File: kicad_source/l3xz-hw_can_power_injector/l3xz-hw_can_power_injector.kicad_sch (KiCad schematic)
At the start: 18 parts, among them CN1 Conn_01x02, CN2 Conn_01x04, CN3 Conn_01x04, CN4 Conn_01x02, U1 RAA211650

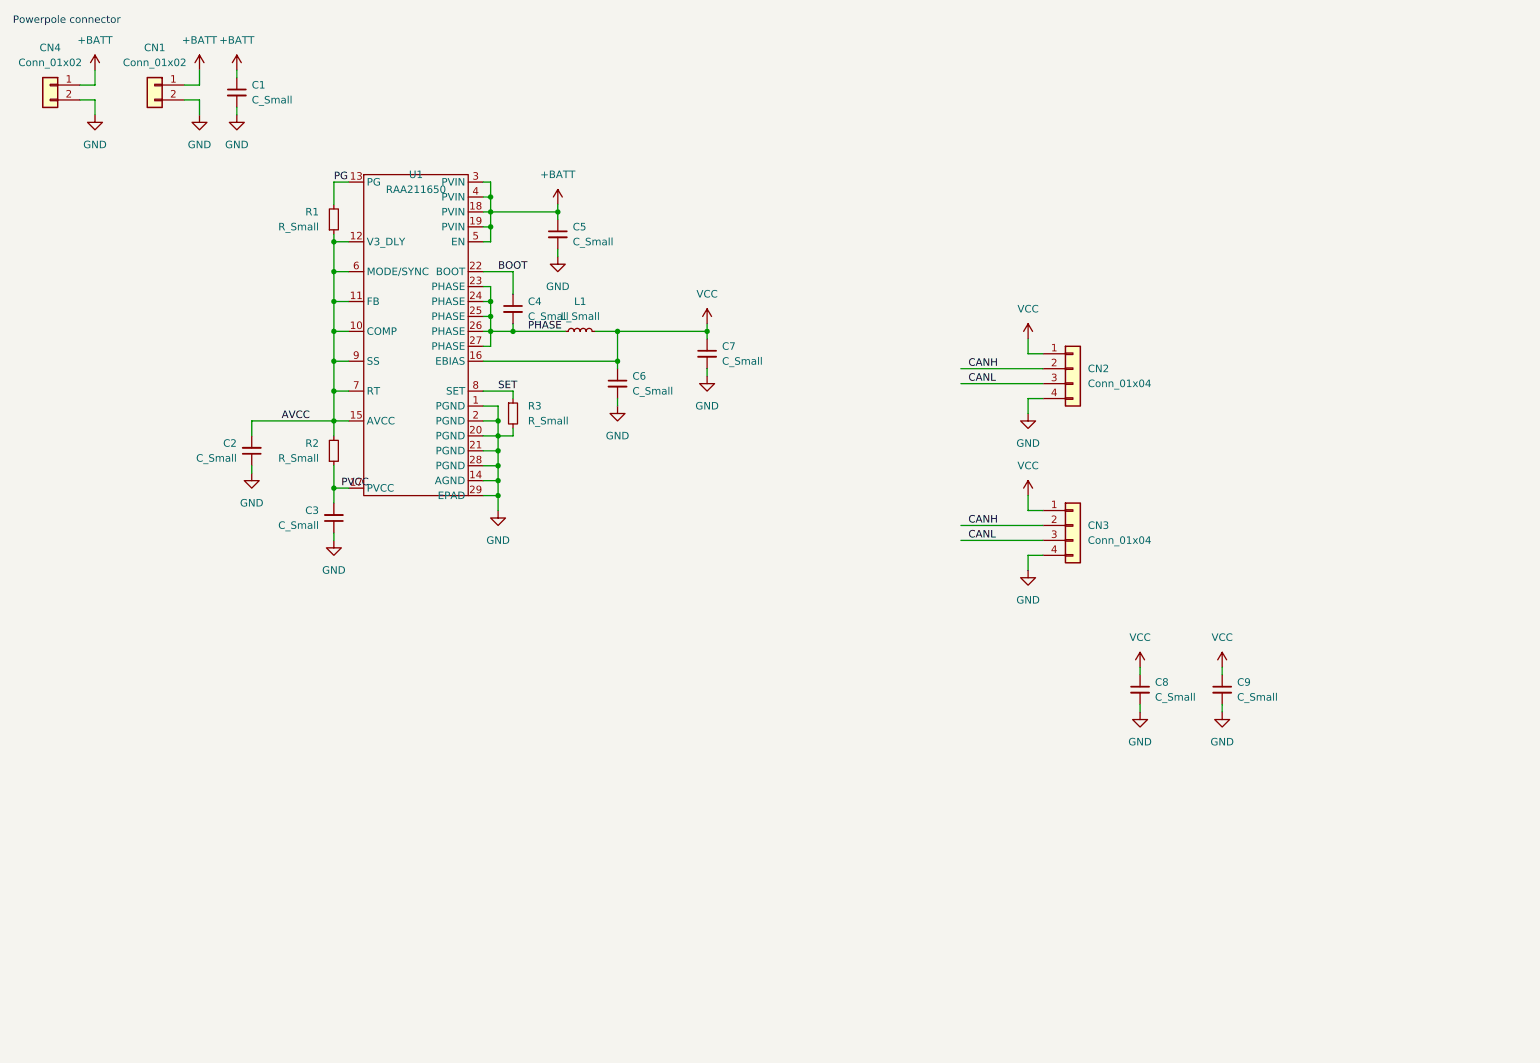
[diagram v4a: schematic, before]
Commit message: addedhoricontal powerpole
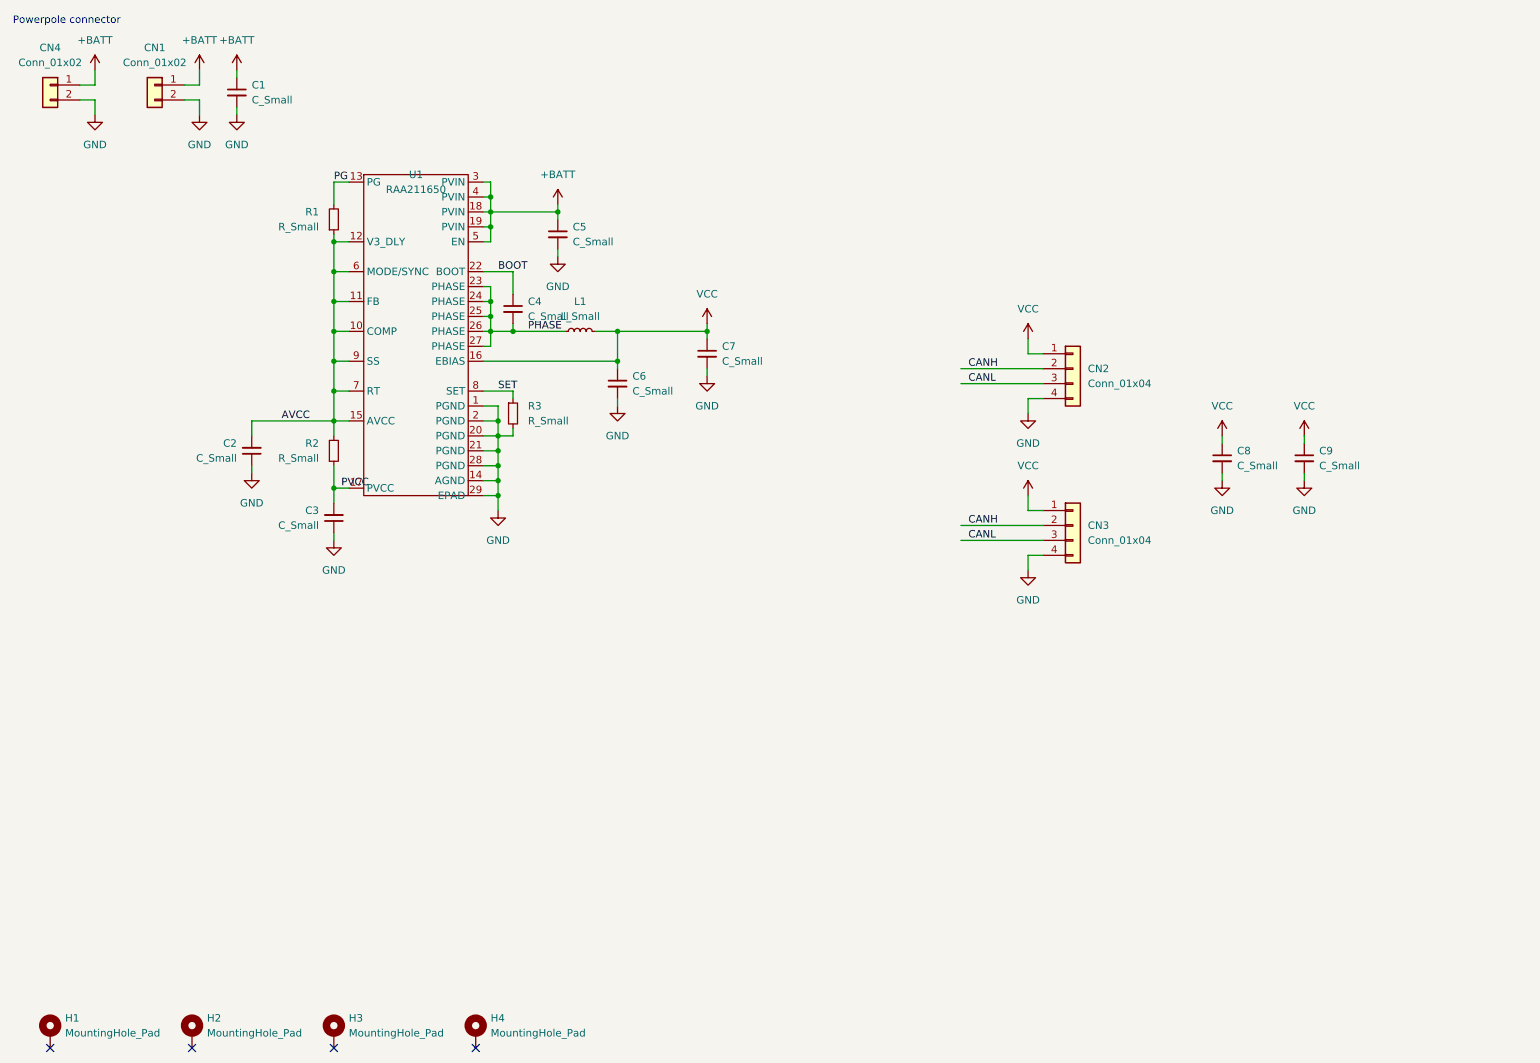
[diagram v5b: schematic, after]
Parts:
- added H1, H2, H3, H4: MountingHole_Pad, MountingHole:MountingHole_3.2mm_M3_DIN965_Pad, symbol Mechanical:MountingHole_Pad
- CN4: footprint generationmake:POWERPOLE_2 -> generationmake:POWERPOLE_hor_2
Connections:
- no-connect marks 0 -> 4
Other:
- moved on the sheet: C8, C9

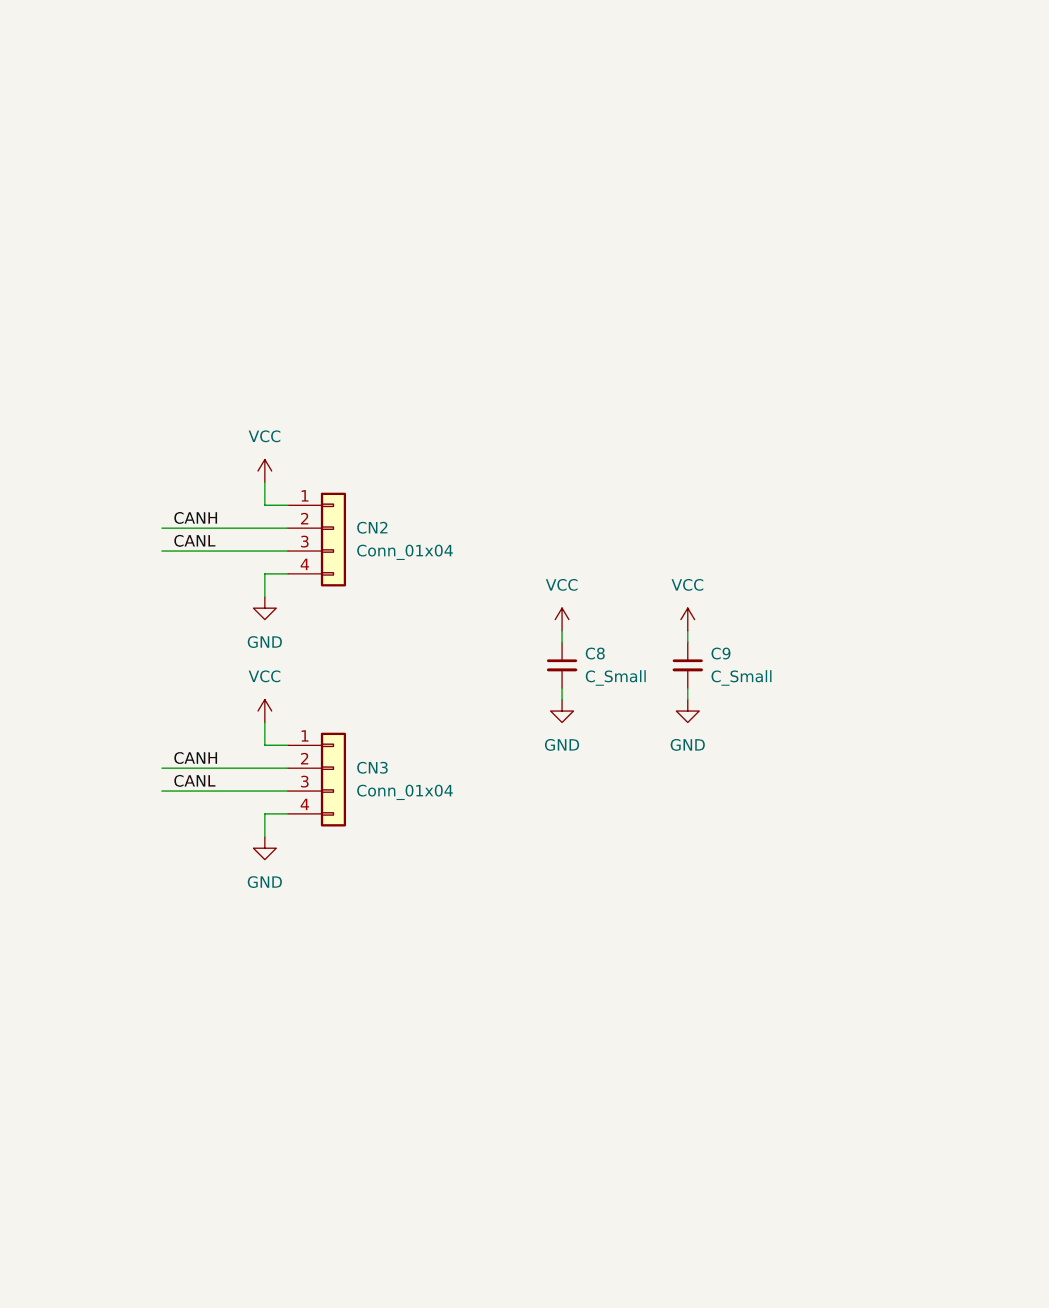
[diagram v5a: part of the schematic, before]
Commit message: added second uavcan channel and diodes
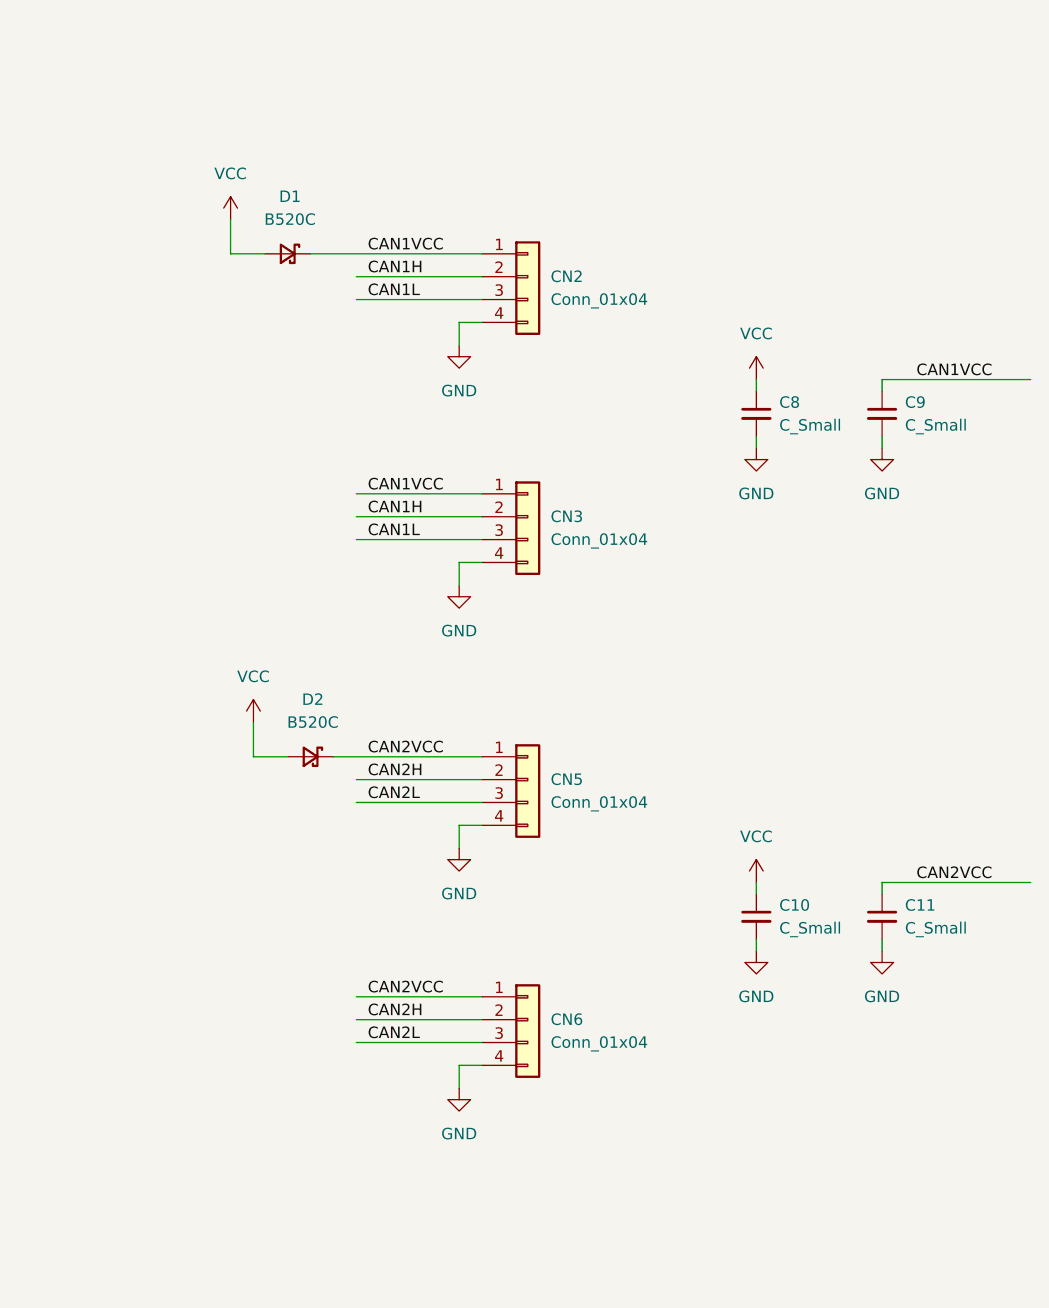
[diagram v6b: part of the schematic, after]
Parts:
- added C10: C_Small, Capacitor_SMD:C_1210_3225Metric, symbol Device:C_Small
- added C11: C_Small, Capacitor_SMD:C_0603_1608Metric, symbol Device:C_Small
- added CN5, CN6: Conn_01x04, Connector_JST:JST_GH_BM04B-GHS-TBT_1x04-1MP_P1.25mm_Vertical, symbol Connector_Generic:Conn_01x04
- added D1, D2: B520C, Diode_SMD:D_SMC, symbol Device:D_Schottky_Small
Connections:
- net GND: now also C10.2, C11.2, CN5.4 (Pin_4), CN6.4 (Pin_4)
- net VCC: now also C10.1, D1.2 (A), D2.2 (A); no longer C9.1, CN2.1 (Pin_1), CN3.1 (Pin_1)
- net CANH renamed CAN1H
- net CANL renamed CAN1L
- new net CAN1VCC: C9.1, CN2.1 (Pin_1), CN3.1 (Pin_1), D1.1 (K)
- new net CAN2H: CN5.2 (Pin_2), CN6.2 (Pin_2)
- new net CAN2L: CN5.3 (Pin_3), CN6.3 (Pin_3)
- new net CAN2VCC: C11.1, CN5.1 (Pin_1), CN6.1 (Pin_1), D2.1 (K)
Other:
- moved on the sheet: C8, C9, CN2, CN3

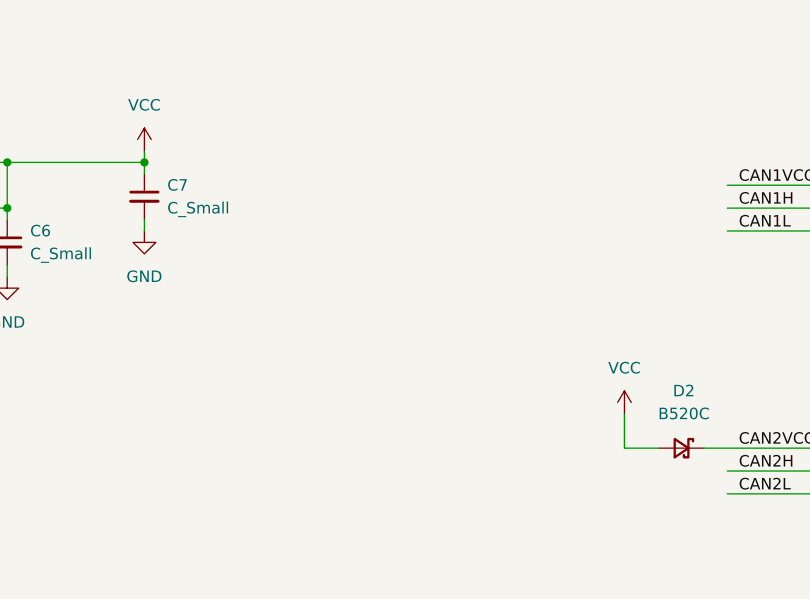
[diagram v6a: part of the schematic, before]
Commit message: added LED
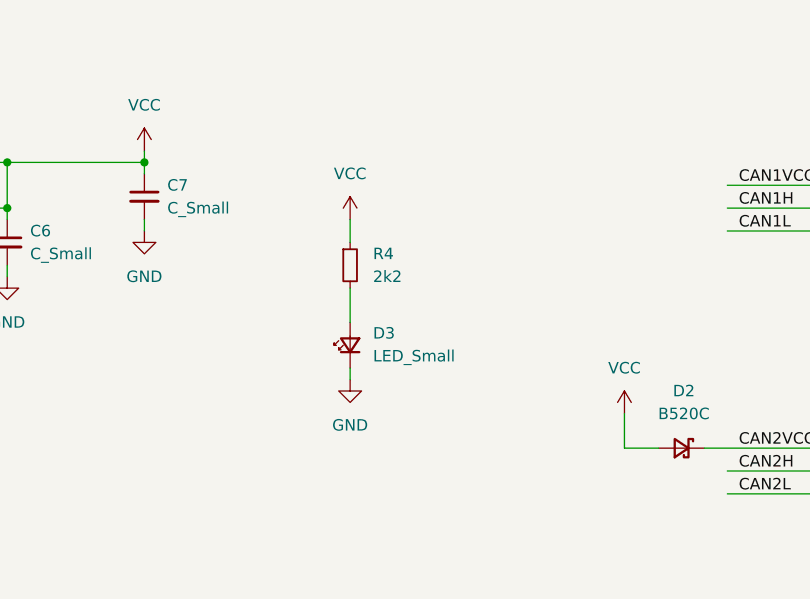
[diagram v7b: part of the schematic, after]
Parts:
- added D3: LED_Small, LED_SMD:LED_0603_1608Metric, symbol Device:LED_Small
- added R4: 2k2, Resistor_SMD:R_0603_1608Metric, symbol Device:R_Small
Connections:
- net GND: now also D3.1 (K)
- net VCC: now also R4.1
- new net: D3.2 (A), R4.2
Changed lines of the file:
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@@
+    (stroke (width 0) (type default) (color 0 0 0 0))
+  )
+  (wire (pts (xy 156.21 83.82) (xy 156.21 87.63))
     (stroke (width 0) (type default) (color 0 0 0 0))
   )
@@
     (stroke (width 0) (type default) (color 0 0 0 0))
   )
+  (wire (pts (xy 156.21 92.71) (xy 156.21 93.98))
+    (stroke (width 0) (type default) (color 0 0 0 0))
+  )
   (wire (pts (xy 96.52 52.07) (xy 96.52 49.53))
     (stroke (width 0) (type default) (color 0 0 0 0))
@@
   )
   (wire (pts (xy 198.12 48.26) (xy 212.09 48.26))
+    (stroke (width 0) (type default) (color 0 0 0 0))
+  )
+  (wire (pts (xy 156.21 76.2) (xy 156.21 78.74))
     (stroke (width 0) (type default) (color 0 0 0 0))
   )
@@
     )
     (property "Datasheet" "~" (id 3) (at 69.85 101.6 0)
+      (effects (font (size 1.27 1.27)) hide)
+    )
+    (pin "1")
+    (pin "2")
+  )
+  (symbol (lib_id "Device:LED_Small") (at 156.21 90.17 90) (unit 1)
+    (in_bom yes) (on_board yes) (fields_autoplaced)
+    (property "Reference" "D3" (id 0) (at 158.75 88.8364 90)
+      (effects (font (size 1.27 1.27)) (justify right))
+    )
+    (property "Value" "LED_Small" (id 1) (at 158.75 91.3764 90)
+      (effects (font (size 1.27 1.27)) (justify right))
+    )
+    (property "Footprint" "LED_SMD:LED_0603_1608Metric" (id 2) (at 156.21 90.17 90)
+      (effects (font (size 1.27 1.27)) hide)
+    )
+    (property "Datasheet" "~" (id 3) (at 156.21 90.17 90)
       (effects (font (size 1.27 1.27)) hide)
     )
@@
     (pin "2")
   )
+  (symbol (lib_id "power:VCC") (at 156.21 76.2 0) (unit 1)
+    (in_bom yes) (on_board yes) (fields_autoplaced)
+    (property "Reference" "#PWR019" (id 0) (at 156.21 80.01 0)
+      (effects (font (size 1.27 1.27)) hide)
+    )
+    (property "Value" "VCC" (id 1) (at 156.21 71.12 0))
+    (property "Footprint" "" (id 2) (at 156.21 76.2 0)
+      (effects (font (size 1.27 1.27)) hide)
+    )
+    (property "Datasheet" "" (id 3) (at 156.21 76.2 0)
+      (effects (font (size 1.27 1.27)) hide)
+    )
+    (pin "1")
+  )
+  (symbol (lib_id "power:GND") (at 156.21 93.98 0) (unit 1)
+    (in_bom yes) (on_board yes) (fields_autoplaced)
+    (property "Reference" "#PWR023" (id 0) (at 156.21 100.33 0)
+      (effects (font (size 1.27 1.27)) hide)
+    )
+    (property "Value" "GND" (id 1) (at 156.21 99.06 0))
+    (property "Footprint" "" (id 2) (at 156.21 93.98 0)
+      (effects (font (size 1.27 1.27)) hide)
+    )
+    (property "Datasheet" "" (id 3) (at 156.21 93.98 0)
+      (effects (font (size 1.27 1.27)) hide)
+    )
+    (pin "1")
+  )
   (symbol (lib_id "Device:R_Small") (at 69.85 50.8 0) (mirror x) (unit 1)
     (in_bom yes) (on_board yes) (fields_autoplaced)
@@
     )
     (pin "1")
+  )
+  (symbol (lib_id "Device:R_Small") (at 156.21 81.28 0) (unit 1)
+    (in_bom yes) (on_board yes) (fields_autoplaced)
+    (property "Reference" "R4" (id 0) (at 158.75 80.0099 0)
+      (effects (font (size 1.27 1.27)) (justify left))
+    )
+    (property "Value" "2k2" (id 1) (at 158.75 82.5499 0)
+      (effects (font (size 1.27 1.27)) (justify left))
+    )
+    (property "Footprint" "Resistor_SMD:R_0603_1608Metric" (id 2) (at 156.21 81.28 0)
+      (effects (font (size 1.27 1.27)) hide)
+    )
+    (property "Datasheet" "~" (id 3) (at 156.21 81.28 0)
+      (effects (font (size 1.27 1.27)) hide)
+    )
+    (pin "1")
+    (pin "2")
   )
   (symbol (lib_id "power:+BATT") (at 53.34 25.4 0) (unit 1)
@@
       (reference "#PWR018") (unit 1) (value "GND") (footprint "")
     )
+    (path "/9f110114-cd8f-4e65-8192-9f1a1a9f677a"
+      (reference "#PWR019") (unit 1) (value "VCC") (footprint "")
+    )
     (path "/650546c7-f011-4983-8eff-739b4d8ccb25"
       (reference "#PWR020") (unit 1) (value "GND") (footprint "")
@@
       (reference "#PWR022") (unit 1) (value "GND") (footprint "")
     )
+    (path "/a32052cf-734b-409d-9f22-d77f7141df2e"
+      (reference "#PWR023") (unit 1) (value "GND") (footprint "")
+    )
     (path "/9843e567-1cac-4c7b-aea1-3d5399a62520"
       (reference "#PWR024") (unit 1) (value "GND") (footprint "")
@@
       (reference "D2") (unit 1) (value "B520C") (footprint "Diode_SMD:D_SMC")
     )
+    (path "/2cb2d04c-0cc5-487d-8f84-20c79a27fb91"
+      (reference "D3") (unit 1) (value "LED_Small") (footprint "LED_SMD:LED_0603_1608Metric")
+    )
     (path "/1e5f82a3-3ad8-404f-a262-3c0e3dd26392"
       (reference "H1") (unit 1) (value "MountingHole_Pad") (footprint "MountingHole:MountingHole_3.2mm_M3_DIN965_Pad")
@@
       (reference "R3") (unit 1) (value "R_Small") (footprint "Resistor_SMD:R_0603_1608Metric")
     )
+    (path "/dfb89183-29f2-4a98-8169-f1a71ef56a26"
+      (reference "R4") (unit 1) (value "2k2") (footprint "Resistor_SMD:R_0603_1608Metric")
+    )
     (path "/65f8fcbf-9a3e-4454-8669-cf6872197858"
